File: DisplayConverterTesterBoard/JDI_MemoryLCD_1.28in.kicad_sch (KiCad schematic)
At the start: 0 parts

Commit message: added FPC connector for 1.28in
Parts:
- added J?: Conn_01x10_MountingPin, Connector_FFC-FPC:Hirose_FH12-10S-0.5SH_1x10-1MP_P0.50mm_Horizontal, symbol Connector_Generic_MountingPin:Conn_01x10_MountingPin
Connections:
- new net DISP: J?.5 (Pin_5)
- new net EXTCOMMIN: J?.4 (Pin_4)
- new net EXTMODE: J?.8 (Pin_8)
- new net MOSI: J?.2 (Pin_2)
- new net SCK: J?.1 (Pin_1)
- new net VDD: J?.7 (Pin_7)
- new net VDDA: J?.6 (Pin_6)
- new net VSS: J?.9 (Pin_9)
- new net VSSA: J?.10 (Pin_10)
- new net ~{SCS}: J?.3 (Pin_3)
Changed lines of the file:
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@@
 (kicad_sch (version 20230121) (generator eeschema)
   (paper "A4")
+  (wire (pts (xy 85.09 77.47) (xy 93.98 77.47))
+    (stroke (width 0) (type default))
+  )
+  (wire (pts (xy 85.09 69.85) (xy 93.98 69.85))
+    (stroke (width 0) (type default))
+  )
+  (wire (pts (xy 85.09 72.39) (xy 93.98 72.39))
+    (stroke (width 0) (type default))
+  )
+  (wire (pts (xy 85.09 59.69) (xy 93.98 59.69))
+    (stroke (width 0) (type default))
+  )
+  (wire (pts (xy 85.09 67.31) (xy 93.98 67.31))
+    (stroke (width 0) (type default))
+  )
+  (wire (pts (xy 85.09 80.01) (xy 93.98 80.01))
+    (stroke (width 0) (type default))
+  )
+  (wire (pts (xy 85.09 57.15) (xy 93.98 57.15))
+    (stroke (width 0) (type default))
+  )
+  (wire (pts (xy 85.09 64.77) (xy 93.98 64.77))
+    (stroke (width 0) (type default))
+  )
+  (wire (pts (xy 85.09 74.93) (xy 93.98 74.93))
+    (stroke (width 0) (type default))
+  )
+  (wire (pts (xy 85.09 62.23) (xy 93.98 62.23))
+    (stroke (width 0) (type default))
+  )
+  (label "EXTCOMMIN" (at 93.98 64.77 0) (fields_autoplaced)
+    (effects (font (size 1.27 1.27)) (justify left bottom))
+  )
+  (label "SCK" (at 93.98 57.15 0) (fields_autoplaced)
+    (effects (font (size 1.27 1.27)) (justify left bottom))
+  )
+  (label "EXTMODE" (at 93.98 74.93 0) (fields_autoplaced)
+    (effects (font (size 1.27 1.27)) (justify left bottom))
+  )
+  (label "VDD" (at 93.98 72.39 0) (fields_autoplaced)
+    (effects (font (size 1.27 1.27)) (justify left bottom))
+  )
+  (label "VSS" (at 93.98 77.47 0) (fields_autoplaced)
+    (effects (font (size 1.27 1.27)) (justify left bottom))
+  )
+  (label "MOSI" (at 93.98 59.69 0) (fields_autoplaced)
+    (effects (font (size 1.27 1.27)) (justify left bottom))
+  )
+  (label "DISP" (at 93.98 67.31 0) (fields_autoplaced)
+    (effects (font (size 1.27 1.27)) (justify left bottom))
+  )
+  (label "VDDA" (at 93.98 69.85 0) (fields_autoplaced)
+    (effects (font (size 1.27 1.27)) (justify left bottom))
+  )
+  (label "VSSA" (at 93.98 80.01 0) (fields_autoplaced)
+    (effects (font (size 1.27 1.27)) (justify left bottom))
+  )
+  (label "~{SCS}" (at 93.98 62.23 0) (fields_autoplaced)
+    (effects (font (size 1.27 1.27)) (justify left bottom))
+  )
+  (symbol (lib_id "Connector_Generic_MountingPin:Conn_01x10_MountingPin") (at 80.01 67.31 0) (mirror y) (unit 1)
+    (in_bom yes) (on_board yes) (dnp no) (fields_autoplaced)
+    (property "Reference" "J?" (at 80.01 50.8 0)
+      (effects (font (size 1.27 1.27)))
+    )
+    (property "Value" "Conn_01x10_MountingPin" (at 80.01 53.34 0)
+      (effects (font (size 1.27 1.27)))
+    )
+    (property "Footprint" "Connector_FFC-FPC:Hirose_FH12-10S-0.5SH_1x10-1MP_P0.50mm_Horizontal" (at 80.01 67.31 0)
+      (effects (font (size 1.27 1.27)) hide)
+    )
+    (property "Datasheet" "~" (at 80.01 67.31 0)
+      (effects (font (size 1.27 1.27)) hide)
+    )
+    (pin "1")
+    (pin "10")
+    (pin "2")
+    (pin "3")
+    (pin "4")
+    (pin "5")
+    (pin "6")
+    (pin "7")
+    (pin "8")
+    (pin "9")
+    (pin "MP")
+    (instances
+      (project "DisplayConverterTesterBoard"
+        (path "/58d9d6aa-d5e3-4b7b-b546-d57c329de758/0cb4f2ca-84b3-4b7f-ac05-316b1c40137b"
+          (reference "J?") (unit 1)
+        )
+      )
+    )
+  )
 )

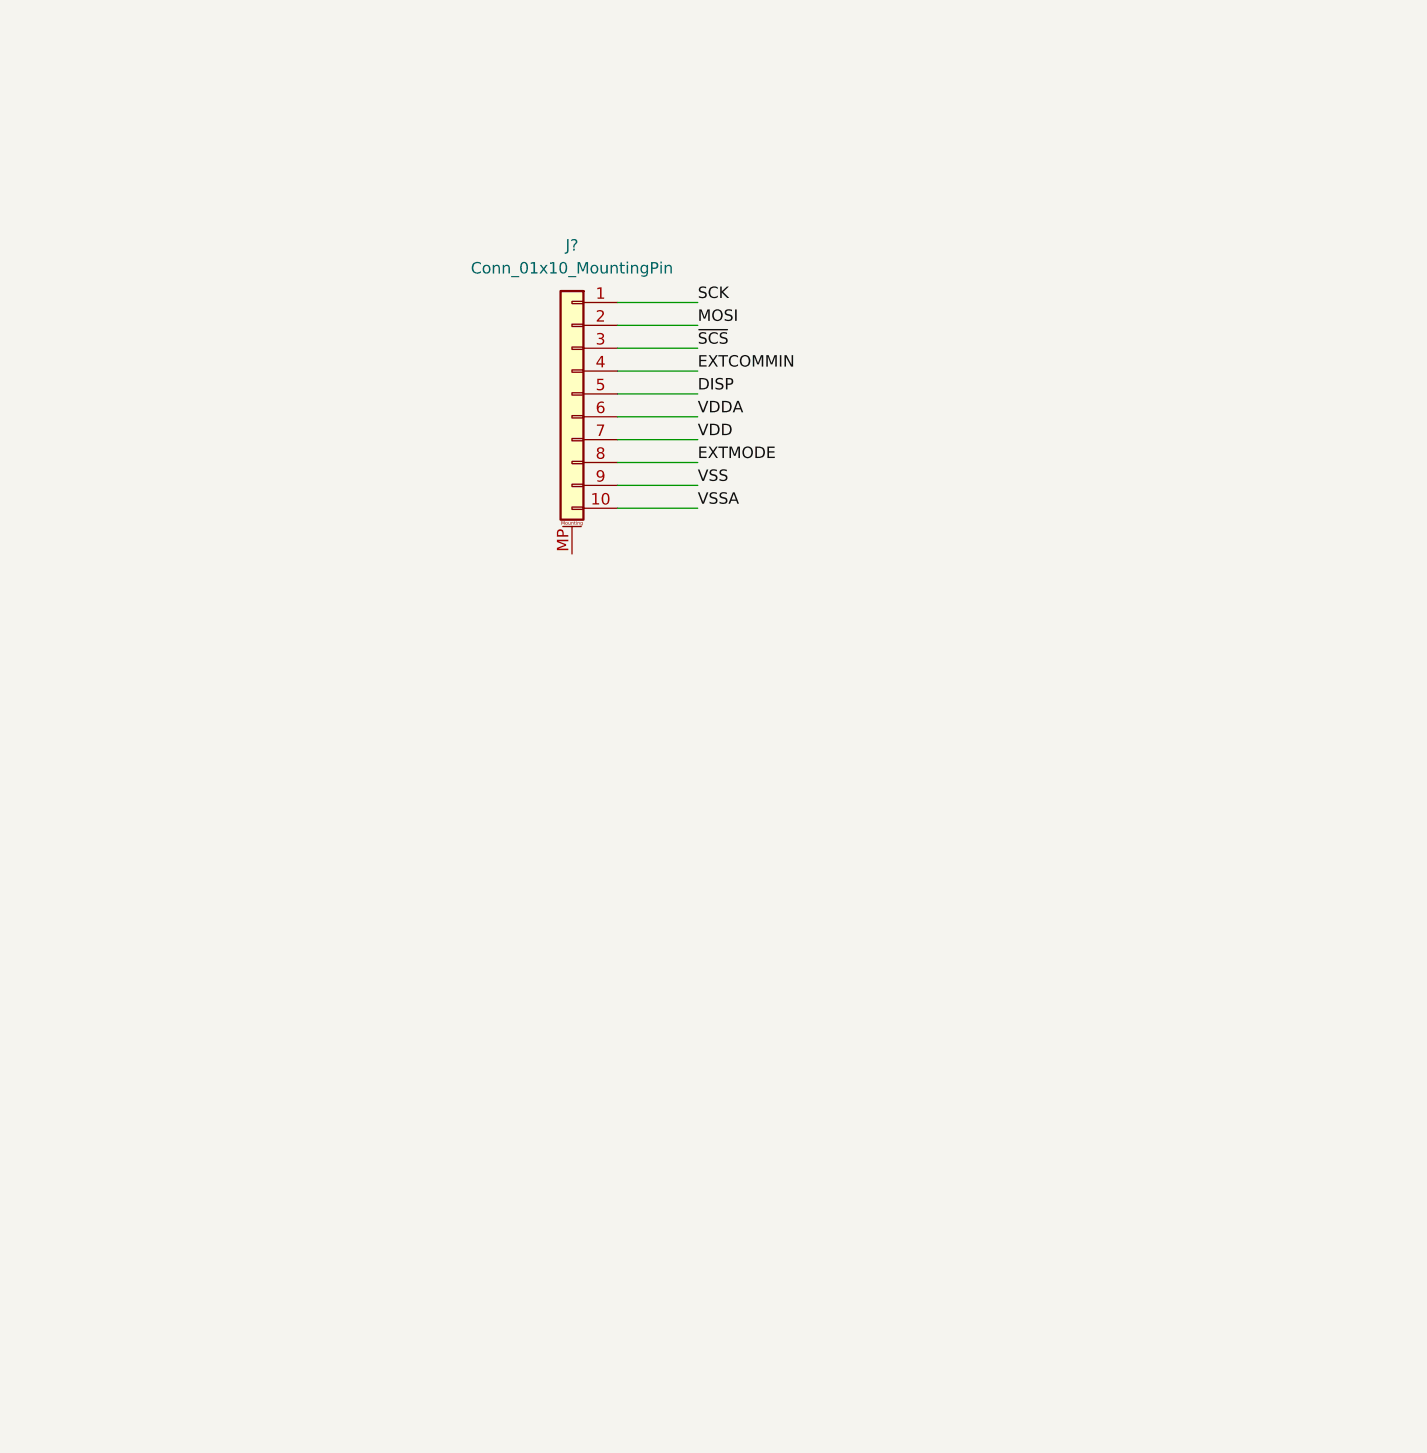
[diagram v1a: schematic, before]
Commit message: updated pinout
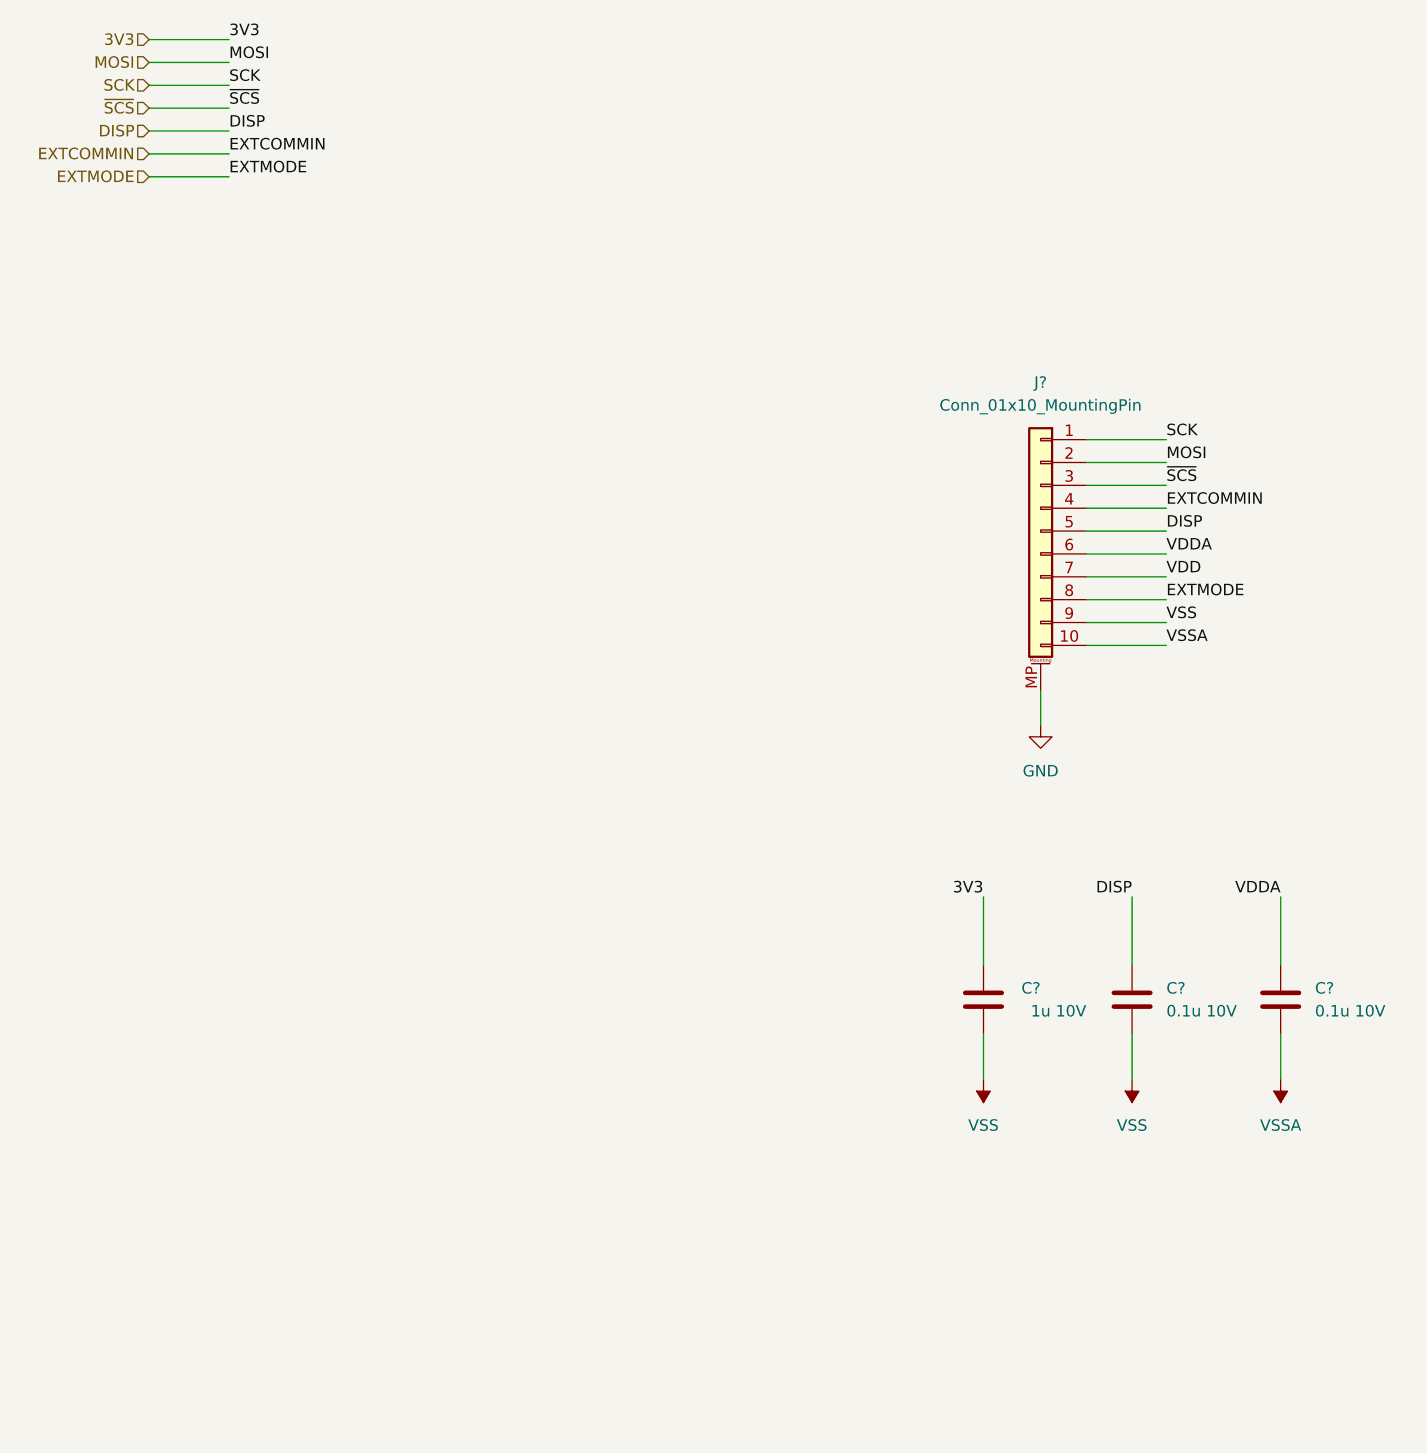
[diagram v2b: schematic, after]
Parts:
- added C? (x2): 0.1u 10V, symbol Device:C
- added C?: 1u 10V, symbol Device:C
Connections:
- net DISP: now also C?.1
- net VDDA: now also C?.1
- net VSS: now also C?.2, C?.2
- net VSSA: now also C?.2
- net GND: now reaches J?.MP (MountPin)
- new net 3V3: C?.1
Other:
- moved on the sheet: J?
